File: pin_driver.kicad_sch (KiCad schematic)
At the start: 3 parts, among them Q501 2N7002

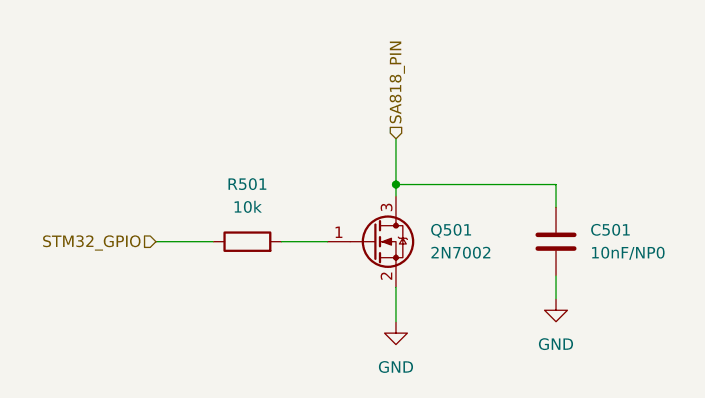
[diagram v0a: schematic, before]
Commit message: update stm32, add some new 3d files
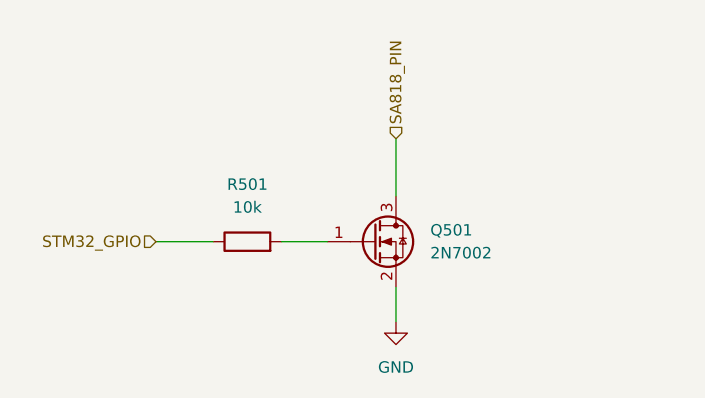
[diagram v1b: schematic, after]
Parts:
- removed C501: 10nF/NP0, Capacitor_SMD:C_0805_2012Metric, symbol Device:C
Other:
- title: Pin Driver for the SA818 -> Pin Driver for the SA818 MOSFET
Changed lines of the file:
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@@
 	(paper "A4")
 	(title_block
-		(title "Pin Driver for the SA818")
+		(title "Pin Driver for the SA818 MOSFET")
 		(rev "<<HASH>>")
 		(company "Amateurfunkclub für Remote Stationen")
 	)
-	(junction
-		(at 143.51 83.82)
-		(diameter 0)
-		(color 0 0 0 0)
-	)
-	(wire
-		(pts
-			(xy 161.29 93.98) (xy 161.29 96.52)
-		)
-		(stroke
-			(width 0)
-			(type default)
-		)
-	)
-	(wire
-		(pts
-			(xy 161.29 86.36) (xy 161.29 83.82)
-		)
-		(stroke
-			(width 0)
-			(type default)
-		)
-	)
-	(wire
-		(pts
-			(xy 143.51 83.82) (xy 143.51 85.09)
+	(wire
+		(pts
+			(xy 143.51 78.74) (xy 143.51 85.09)
 		)
 		(stroke
@@
 	(wire
 		(pts
-			(xy 143.51 78.74) (xy 143.51 83.82)
-		)
-		(stroke
-			(width 0)
-			(type default)
-		)
-	)
-	(wire
-		(pts
 			(xy 143.51 95.25) (xy 143.51 99.06)
-		)
-		(stroke
-			(width 0)
-			(type default)
-		)
-	)
-	(wire
-		(pts
-			(xy 143.51 83.82) (xy 161.29 83.82)
 		)
 		(stroke
@@
 			)
 			(justify right)
-		)
-	)
-	(symbol
-		(lib_id "power:GND")
-		(at 161.29 96.52 0)
-		(unit 1)
-		(exclude_from_sim no)
-		(in_bom yes)
-		(on_board yes)
-		(dnp no)
-		(fields_autoplaced yes)
-		(property "Reference" "#PWR0502"
-			(at 161.29 102.87 0)
-			(effects
-				(font
-					(size 1.27 1.27)
-				)
-				(hide yes)
-			)
-		)
-		(property "Value" "GND"
-			(at 161.29 101.6 0)
-			(effects
-				(font
-					(size 1.27 1.27)
-				)
-			)
-		)
-		(property "Footprint" ""
-			(at 161.29 96.52 0)
-			(effects
-				(font
-					(size 1.27 1.27)
-				)
-				(hide yes)
-			)
-		)
-		(property "Datasheet" ""
-			(at 161.29 96.52 0)
-			(effects
-				(font
-					(size 1.27 1.27)
-				)
-				(hide yes)
-			)
-		)
-		(property "Description" "Power symbol creates a global label with name \"GND\" , ground"
-			(at 161.29 96.52 0)
-			(effects
-				(font
-					(size 1.27 1.27)
-				)
-				(hide yes)
-			)
-		)
-		(pin "1"
-		)
-		(instances
-			(project "fm"
-				(path "/f228839c-6576-40b2-ae70-679b7b460639/03cdba2c-ce18-41b8-ae87-2767326fecab"
-					(reference "#PWR0604")
-					(unit 1)
-				)
-				(path "/f228839c-6576-40b2-ae70-679b7b460639/0ab8e43f-a9b2-43d4-be36-1f1ef25ab18a"
-					(reference "#PWR0502")
-					(unit 1)
-				)
-				(path "/f228839c-6576-40b2-ae70-679b7b460639/9b9e5cf7-8c6a-4bb3-8c33-fcdf0be9d0fd"
-					(reference "#PWR0602")
-					(unit 1)
-				)
-			)
 		)
 	)
@@
 		(instances
 			(project "fm"
-				(path "/f228839c-6576-40b2-ae70-679b7b460639/03cdba2c-ce18-41b8-ae87-2767326fecab"
-					(reference "R701")
-					(unit 1)
-				)
 				(path "/f228839c-6576-40b2-ae70-679b7b460639/0ab8e43f-a9b2-43d4-be36-1f1ef25ab18a"
 					(reference "R501")
-					(unit 1)
-				)
-				(path "/f228839c-6576-40b2-ae70-679b7b460639/9b9e5cf7-8c6a-4bb3-8c33-fcdf0be9d0fd"
-					(reference "R601")
 					(unit 1)
 				)
@@
 		(instances
 			(project "fm"
-				(path "/f228839c-6576-40b2-ae70-679b7b460639/03cdba2c-ce18-41b8-ae87-2767326fecab"
-					(reference "#PWR0603")
-					(unit 1)
-				)
 				(path "/f228839c-6576-40b2-ae70-679b7b460639/0ab8e43f-a9b2-43d4-be36-1f1ef25ab18a"
 					(reference "#PWR0501")
-					(unit 1)
-				)
-				(path "/f228839c-6576-40b2-ae70-679b7b460639/9b9e5cf7-8c6a-4bb3-8c33-fcdf0be9d0fd"
-					(reference "#PWR0601")
-					(unit 1)
-				)
-			)
-		)
-	)
-	(symbol
-		(lib_id "Device:C")
-		(at 161.29 90.17 180)
-		(unit 1)
-		(exclude_from_sim no)
-		(in_bom yes)
-		(on_board yes)
-		(dnp no)
-		(fields_autoplaced yes)
-		(property "Reference" "C501"
-			(at 165.1 88.8999 0)
-			(effects
-				(font
-					(size 1.27 1.27)
-				)
-				(justify right)
-			)
-		)
-		(property "Value" "10nF/NP0"
-			(at 165.1 91.4399 0)
-			(effects
-				(font
-					(size 1.27 1.27)
-				)
-				(justify right)
-			)
-		)
-		(property "Footprint" "Capacitor_SMD:C_0805_2012Metric"
-			(at 160.3248 86.36 0)
-			(effects
-				(font
-					(size 1.27 1.27)
-				)
-				(hide yes)
-			)
-		)
-		(property "Datasheet" "~"
-			(at 161.29 90.17 0)
-			(effects
-				(font
-					(size 1.27 1.27)
-				)
-				(hide yes)
-			)
-		)
-		(property "Description" "Unpolarized capacitor"
-			(at 161.29 90.17 0)
-			(effects
-				(font
-					(size 1.27 1.27)
-				)
-				(hide yes)
-			)
-		)
-		(property "LCSC" ""
-			(at 161.29 90.17 0)
-			(effects
-				(font
-					(size 1.27 1.27)
-				)
-				(hide yes)
-			)
-		)
-		(property "MOUSER" "81-GRM2165C2A103JA1D"
-			(at 161.29 90.17 0)
-			(effects
-				(font
-					(size 1.27 1.27)
-				)
-				(hide yes)
-			)
-		)
-		(pin "1"
-		)
-		(pin "2"
-		)
-		(instances
-			(project "fm"
-				(path "/f228839c-6576-40b2-ae70-679b7b460639/03cdba2c-ce18-41b8-ae87-2767326fecab"
-					(reference "C701")
-					(unit 1)
-				)
-				(path "/f228839c-6576-40b2-ae70-679b7b460639/0ab8e43f-a9b2-43d4-be36-1f1ef25ab18a"
-					(reference "C501")
-					(unit 1)
-				)
-				(path "/f228839c-6576-40b2-ae70-679b7b460639/9b9e5cf7-8c6a-4bb3-8c33-fcdf0be9d0fd"
-					(reference "C601")
 					(unit 1)
 				)
@@
 			)
 		)
+		(property "LCSC" ""
+			(at 140.97 90.17 0)
+			(effects
+				(font
+					(size 1.27 1.27)
+				)
+				(hide yes)
+			)
+		)
 		(pin "1"
 		)
@@
 		(instances
 			(project "fm"
-				(path "/f228839c-6576-40b2-ae70-679b7b460639/03cdba2c-ce18-41b8-ae87-2767326fecab"
-					(reference "Q701")
-					(unit 1)
-				)
 				(path "/f228839c-6576-40b2-ae70-679b7b460639/0ab8e43f-a9b2-43d4-be36-1f1ef25ab18a"
 					(reference "Q501")
 					(unit 1)
 				)
-				(path "/f228839c-6576-40b2-ae70-679b7b460639/9b9e5cf7-8c6a-4bb3-8c33-fcdf0be9d0fd"
-					(reference "Q601")
-					(unit 1)
-				)

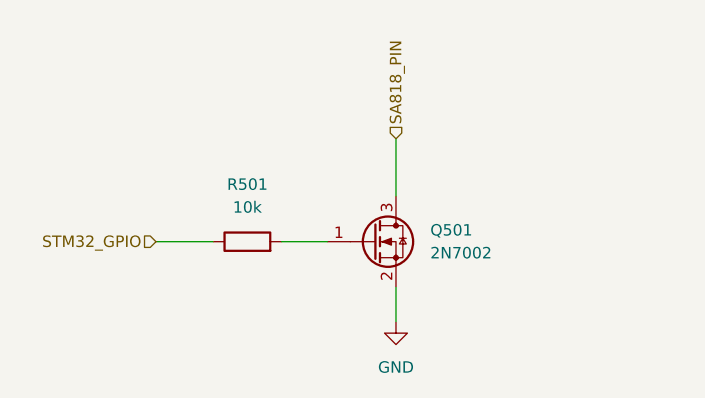
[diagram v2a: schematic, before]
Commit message: Fix transistor symbol visibility and update polyline coordinates in schematic
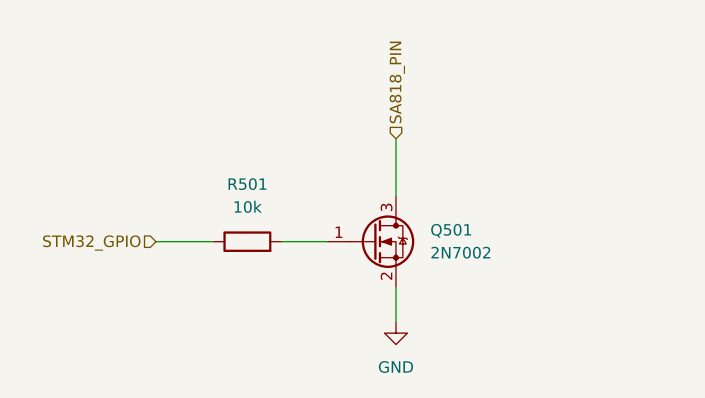
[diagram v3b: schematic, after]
